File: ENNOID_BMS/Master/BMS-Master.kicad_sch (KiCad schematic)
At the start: 32 parts, among them J1 Contactor+, J10 Charge, J11 CAN, J12 USB, J16 ISOSPI, J18 OLED, J19 ISOSPI, J2 Cooling, J3 + 12V -, J4 Contactor-, J5 Power, J6 Power Button, J7 E-Stop, J8 Discharge, J9 Discharge, K1 SHV12-1A85-78L3K, Q1 BSS138

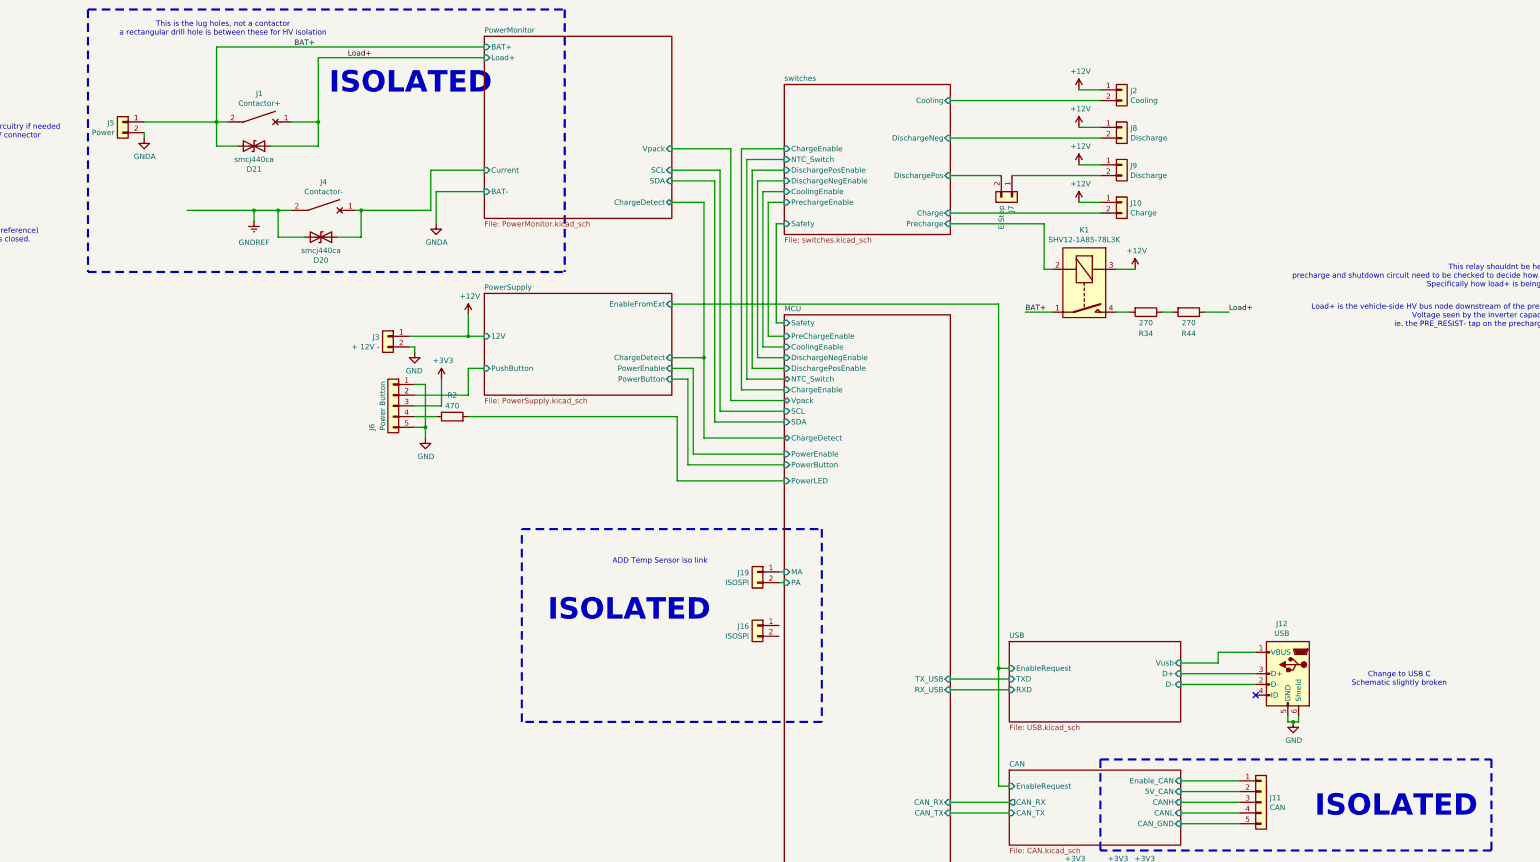
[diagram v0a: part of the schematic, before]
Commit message: updated breakout
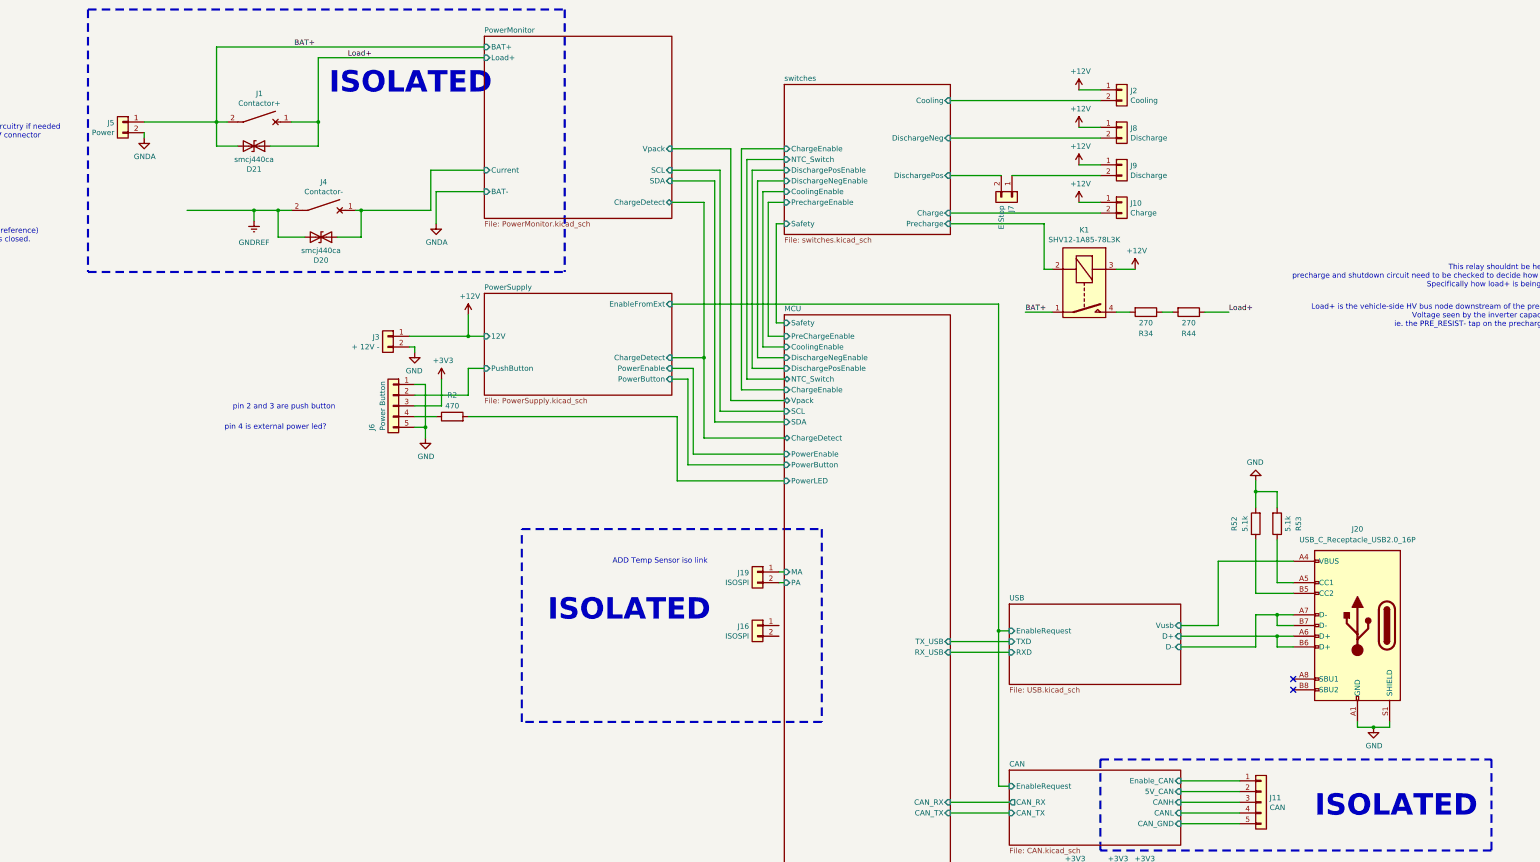
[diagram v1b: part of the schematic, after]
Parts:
- removed J12: USB, Connector_USB:USB_Micro-B_Molex-105133-0001, symbol BMS-Master-rescue:USB_B_Micro-Connector_Specialized-BMS-Master-rescue
- added J20: USB_C_Receptacle_USB2.0_16P, symbol Connector:USB_C_Receptacle_USB2.0_16P
- added R52, R53: 5.1k, Resistor_SMD:R_0603_1608Metric, symbol BMS-Master-rescue:R-Device-BMS-Master-rescue
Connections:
- net GND: now also J20.A1 (GND), J20.A12 (GND), J20.B1 (GND), J20.B12 (GND), J20.S1 (SHIELD), R52.2, R53.2
- net USB/D+: now also J20.A6 (D+), J20.B6 (D+)
- net USB/D-: now also J20.A7 (D-), J20.B7 (D-)
- net USB/Vusb: now also J20.A4 (VBUS), J20.A9 (VBUS), J20.B4 (VBUS), J20.B9 (VBUS)
- new net: J20.A5 (CC1), R53.1
- new net: J20.B5 (CC2), R52.1
- no-connect marks 1 -> 2
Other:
- note added: "pin 2 and 3 are push button"
- note added: "pin 4 is external power led?"
- note removed: "Change to USB C Schematic slightly broken"
- note removed: "This is the lug holes, not a contactor a rectangular drill hole is between these for HV isolation"

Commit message: ENNOID BMS PCBs completed
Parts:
- added J21: INV_Power, Connector_Phoenix_GMSTB:PhoenixContact_GMSTBVA_2,5_2-G_1x02_P7.50mm_Vertical, symbol BMS-Master-rescue:Conn_01x02-Connector_Generic-BMS-Master-rescue
- J11, J18, J6: footprint Connectors_Molex:Molex_KK-6410-05_05x2.54mm_Straight -> Connector_Molex:Molex_KK-254_AE-6410-05A_1x05_P2.54mm_Vertical
- J16: value ISOSPI -> ISOSPI_TEMP
- J19: value ISOSPI -> ISOSPI_CELL
- J20: footprint (none) -> ENNOID:SAMESKY_UJ20-C-H-G-SMT-1-P16-TR
- J5: value Power -> BAT_Power
- Q1: footprint TO_SOT_Packages_SMD:SOT-23 -> Package_TO_SOT_SMD:SOT-23
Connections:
- net GNDREF: now also J21.2 (Pin_2)
- net Load+: now also J21.1 (Pin_1)
- net MCU/MA_TEMP: now reaches J16.1 (Pin_1)
- net MCU/PA_TEMP: now reaches J16.2 (Pin_2)
- net MCU/MA renamed MCU/MA_CELL
- net MCU/PA renamed MCU/PA_CELL
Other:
- sheet MCU ports: added MA_CELL, MA_TEMP, PA_CELL, PA_TEMP; removed MA, PA
- note added: "AIR 1"
- note added: "AIR 2"
- note added: "Goes to all HV PCBs as TS+ and TS-"
- note added: "Goes to precharge and discharge as Load+ and load-"
- note added: "Need to decide on what conditions will replace active low discharge enable and multipurpose enable of the orion to give AMS ok. These enable switches to AIR coils will bypass the SDC which is illegal so they should be removed or ignored. Charger and cooling are presumed to be corrent for now The firmware should be understood in this section to determine what the actual behaviour is"
- note added: "pin 1 and 2 are external push button"
- note added: "pin 3 goes to external led, return path pin 4"
- note added: "this appears to be the precharge relay and resistor. These should not be here and resistor values are questionable This needs to be thought out carefully with existing precharge and shutdown circuit topologies"
- note removed: "ADD Temp Sensor iso link"
- note removed: "Load+ is the vehicle-side HV bus node downstream of the precharge resistor and contactors. Voltage seen by the inverter capacitor ie. the PRE_RESIST- tap on the precharge circuit"
- note removed: "This is for external HV circuitry if needed BAT+ Lug is the HV connector"
- note removed: "This relay shouldnt be here. precharge and shutdown circuit need to be checked to decide how this should be ignored or removed from BMS. Specifically how load+ is being handled"
- note removed: "pin 2 and 3 are push button"
- note removed: "pin 4 is external power led?"
- moved on the sheet: J16, J19

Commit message: bms architecture notes made re charging and discharging
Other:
- note added: "Conditions TBC but generally should look something like this"
- note added: "Cooling doesnt appear to be in the firmware, this is probably something we want the bms to control maybe like cooling_on if: max_cell_temp > threshold OR charging_active"
- note added: "TLDR; discharge and precharge are illegal, cooling and charge can stay"
- note added: "This charge pin can be used as the enable pin of the charger. flow could be teensy requests charge over CAN to the BMS, BMS decides on charge enable and safety conditions, shtudown circuit closes, and charger enable switch goes high/low"
- note added: "This is for debugging screen probably not necessary"
- note added: "charger should have additional signals with these conditions to create AMS ok signal for charger shutdown circuit CHARGE_ENABLE_N = active-low "pack may accept charge" = chargeAllowed AND no critical fault CHARGER_SAFETY_N = active-low "external charger may run" = charger_detected AND charging_state_active AND chargeAllowed AND master_ok"
- note added: "discharge should be replaced with new conditions to match the orion and what the shutdown circuit expects they should be active low DISCHARGE_ENABLE_N This should represent battery safe to discharge, with the following conditions: dischargeAllowed AND packInSOA AND all slaves communicating AND no open wire faults AND cell voltage within limits AND temperature within limits MULTIPURPOSE_ENABLE_N T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"
- note added: "this relay can be cut"
- note removed: "Need to decide on what conditions will replace active low discharge enable and multipurpose enable of the orion to give AMS ok. These enable switches to AIR coils will bypass the SDC which is illegal so they should be removed or ignored. Charger and cooling are presumed to be corrent for now The firmware should be understood in this section to determine what the actual behaviour is"
- note removed: "This necessary?"
- note removed: "this appears to be the precharge relay and resistor. These should not be here and resistor values are questionable This needs to be thought out carefully with existing precharge and shutdown circuit topologies"
- moved on the sheet: D1, R1
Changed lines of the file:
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@@
 		(company "ENNOID")
-	)
-	(text "Need to decide on what conditions will replace active low discharge enable and multipurpose enable of the orion to give AMS ok. \n\nThese enable switches to AIR coils will bypass the SDC which is illegal so they should be removed or ignored. \n\nCharger and cooling are presumed to be corrent for now\n\nThe firmware should be understood in this section to determine what the actual behaviour is"
-		(exclude_from_sim no)
-		(at 346.71 47.244 0)
-		(effects
-			(font
-				(size 1.27 1.27)
-			)
-		)
 	)
 	(text "Ground domains:\n	•	GND: Low-voltage logic ground (MCU, CAN, I²C)\n	•	GNDA: Accumulator negative (BAT−, TS−)\n	•	GNDREF: Vehicle-side HV negative (Load−, inverter DC-link reference)\nGNDA and GNDREF are connected only when the negative AIR is closed."
@@
 		(exclude_from_sim no)
 		(at 24.13 33.782 0)
+		(effects
+			(font
+				(size 1.27 1.27)
+			)
+		)
+	)
+	(text "This charge pin can be used as the enable pin of the charger.\nflow could be teensy requests charge over CAN to the BMS, BMS decides on charge enable and safety conditions,\nshtudown circuit closes, and charger enable switch goes high/low"
+		(exclude_from_sim no)
+		(at 349.504 90.424 0)
+		(effects
+			(font
+				(size 1.27 1.27)
+			)
+		)
+	)
+	(text "Conditions TBC but generally should look something like this"
+		(exclude_from_sim no)
+		(at 424.434 41.402 0)
 		(effects
 			(font
@@
 		)
 	)
-	(text "this appears to be the precharge relay and resistor. These should not be here and resistor values are questionable\nThis needs to be thought out carefully with existing precharge and shutdown circuit topologies"
-		(exclude_from_sim no)
-		(at 351.282 77.216 0)
+	(text "this relay can be cut"
+		(exclude_from_sim no)
+		(at 260.858 94.742 0)
 		(effects
 			(font
@@
 		)
 	)
-	(text "This necessary?\n"
+	(text "This is for debugging screen\nprobably not necessary"
 		(exclude_from_sim no)
 		(at 308.61 235.204 0)
+		(effects
+			(font
+				(size 1.27 1.27)
+			)
+		)
+	)
+	(text "charger should have additional signals with these conditions to create AMS ok signal for charger shutdown circuit\nCHARGE_ENABLE_N  = active-low \"pack may accept charge\"\n                 = chargeAllowed AND no critical fault\n\nCHARGER_SAFETY_N = active-low \"external charger may run\"\n                 = charger_detected\n                   AND charging_state_active\n                   AND chargeAllowed\n                   AND master_ok"
+		(exclude_from_sim no)
+		(at 349.504 74.93 0)
 		(effects
 			(font
@@
 		)
 	)
+	(text "Cooling doesnt appear to be in the firmware, this is probably something we want the bms to control\nmaybe like cooling_on if:\n\nmax_cell_temp > threshold\nOR charging_active"
+		(exclude_from_sim no)
+		(at 333.756 16.002 0)
+		(effects
+			(font
+				(size 1.27 1.27)
+			)
+		)
+	)
+	(text "discharge should be replaced with new conditions to match the orion and what the shutdown circuit expects\nthey should be active low\n\nDISCHARGE_ENABLE_N\n\nThis should represent battery safe to discharge, with the following conditions:\n\ndischargeAllowed AND packInSOA AND all slaves communicating AND no open wire faults \nAND cell voltage within limits AND temperature within limits\n\nMULTIPURPOSE_ENABLE_N\n\nThis should represent Master alive and system operational with the following conditions\n\nMCU running AND watchdog serviced AND no firmware fatal fault AND system initialized"
+		(exclude_from_sim no)
+		(at 342.138 39.624 0)
+		(effects
+			(font
+				(size 1.27 1.27)
+			)
+		)
+	)
 	(text "ISOLATED"
 		(exclude_from_sim no)
@@
 		)
 	)
+	(text "TLDR; discharge and precharge are illegal, cooling and charge can stay"
+		(exclude_from_sim no)
+		(at 346.202 102.362 0)
+		(effects
+			(font
+				(size 1.27 1.27)
+			)
+		)
+	)
 	(junction
 		(at 71.12 40.64)
@@
 	(wire
 		(pts
-			(xy 96.52 274.32) (xy 96.52 276.86)
+			(xy 142.24 275.59) (xy 142.24 278.13)
 		)
 		(stroke
@@
 	(wire
 		(pts
-			(xy 96.52 254) (xy 96.52 256.54)
+			(xy 142.24 255.27) (xy 142.24 257.81)
 		)
 		(stroke
@@
 	(wire
 		(pts
-			(xy 96.52 266.7) (xy 96.52 264.16)
+			(xy 142.24 267.97) (xy 142.24 265.43)
 		)
 		(stroke
@@
 	(symbol
 		(lib_id "BMS-Master-rescue:R-Device-BMS-Master-rescue")
-		(at 96.52 260.35 180)
+		(at 142.24 261.62 180)
 		(unit 1)
 		(exclude_from_sim no)
@@
 		(dnp no)
 		(property "Reference" "R1"
-			(at 91.44 260.35 90)
+			(at 137.16 261.62 90)
 			(effects
 				(font
@@
 		)
 		(property "Value" "470"
-			(at 93.98 260.35 90)
+			(at 139.7 261.62 90)
 			(effects
 				(font
@@
 		)
 		(property "Footprint" "Resistor_SMD:R_0603_1608Metric"
-			(at 98.298 260.35 90)
+			(at 144.018 261.62 90)
 			(effects
 				(font
@@
 		)
 		(property "Datasheet" "~"
-			(at 96.52 260.35 0)
+			(at 142.24 261.62 0)
 			(effects
 				(font
@@
 		)
 		(property "Description" ""
-			(at 96.52 260.35 0)
+			(at 142.24 261.62 0)
 			(effects
 				(font
@@
 		)
 		(property "MPN" "RC0603JR-07470RL"
-			(at 96.52 260.35 0)
+			(at 142.24 261.62 0)
 			(effects
 				(font
@@
 	(symbol
 		(lib_id "BMS-Master-rescue:LED-Device-BMS-Master-rescue")
-		(at 96.52 270.51 90)
+		(at 142.24 271.78 90)
 		(unit 1)
 		(exclude_from_sim no)
@@
 		(dnp no)
 		(property "Reference" "D1"
-			(at 99.4918 269.5448 90)
+			(at 145.2118 270.8148 90)
 			(effects
 				(font
@@
 		)
 		(property "Value" "POWER"
-			(at 99.4918 271.8562 90)
+			(at 145.2118 273.1262 90)
 			(effects
 				(font
@@
 		)
 		(property "Footprint" "LED_SMD:LED_0603_1608Metric"
-			(at 96.52 270.51 0)
+			(at 142.24 271.78 0)
 			(effects
 				(font
@@
 		)
 		(property "Datasheet" "~"
-			(at 96.52 270.51 0)
+			(at 142.24 271.78 0)
 			(effects
 				(font
@@
 		)
 		(property "Description" ""
-			(at 96.52 270.51 0)
+			(at 142.24 271.78 0)
 			(effects
 				(font
@@
 		)
 		(property "MPN" "SML-D12P8WT86C"
-			(at 96.52 270.51 0)
+			(at 142.24 271.78 0)
 			(effects
 				(font
@@
 	(symbol
 		(lib_id "BMS-Master-rescue:GND-power-BMS-Master-rescue")
-		(at 96.52 276.86 0)
+		(at 142.24 278.13 0)
 		(unit 1)
 		(exclude_from_sim no)
@@
 		(dnp no)
 		(property "Reference" "#PWR0102"
-			(at 96.52 283.21 0)
+			(at 142.24 284.48 0)
 			(effects
 				(font
@@
 		)
 		(property "Value" "GND"
-			(at 96.647 281.2542 0)
+			(at 142.367 282.5242 0)
 			(effects
 				(font
@@
 		)
 		(property "Footprint" ""
-			(at 96.52 276.86 0)
+			(at 142.24 278.13 0)
 			(effects
 				(font
@@
 		)
 		(property "Datasheet" ""
-			(at 96.52 276.86 0)
+			(at 142.24 278.13 0)
 			(effects
 				(font
@@
 		)
 		(property "Description" ""
-			(at 96.52 276.86 0)
+			(at 142.24 278.13 0)
 			(effects
 				(font
@@
 	(symbol
 		(lib_id "BMS-Master-rescue:+3.3V-power-BMS-Master-rescue")
-		(at 96.52 254 0)
+		(at 142.24 255.27 0)
 		(unit 1)
 		(exclude_from_sim no)
@@
 		(dnp no)
 		(property "Reference" "#PWR0104"
-			(at 96.52 257.81 0)
+			(at 142.24 259.08 0)
 			(effects
 				(font
@@
 		)
 		(property "Value" "+3V3"
-			(at 96.901 249.6058 0)
+			(at 142.621 250.8758 0)
 			(effects
 				(font
@@
 		)
 		(property "Footprint" ""
-			(at 96.52 254 0)
+			(at 142.24 255.27 0)
 			(effects
 				(font
@@
 		)
 		(property "Datasheet" ""
-			(at 96.52 254 0)
+			(at 142.24 255.27 0)
 			(effects
 				(font
@@
 		)
 		(property "Description" ""
-			(at 96.52 254 0)
-			(effects
-				(font
+			(at 142.24 255.27 0)
+			(effects
+				(font
